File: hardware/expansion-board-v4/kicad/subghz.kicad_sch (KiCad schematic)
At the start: 32 parts, among them J5 U.FL_978, Q2 AO3401A, U10 CC1312R1F3RGZR, Y2 48MHz ABM8W-7pF, Y3 32.768kHz FC-135

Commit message: fix(v4): 晶振负载电容按实测 CL 重算——C19/C20→33pF，C68/C69→18pF
罩哥给出实际买到的三颗晶振型号，CL 全部查实：

    Y1  X322512MSB4SI              CL=20pF     立创/JLCPCB/Evelta 三处一致
    Y2  ABM8W-48.0000MHZ-7-D1X-T3  CL=7pF      型号里的「-7-」就是 CL
    Y3  Q13FC13500004 (FC-135)     CL=12.5pF   Epson 官方 IC 配套页

按 C = (CL − Cstray) × 2、Cstray 取 3pF 重算：

              原值          新值      原偏差              新偏差
    C19/C20   15/15pF   →   33/33pF   -9.50pF ≈ 95ppm    -0.50pF ≈ 5ppm
    C68/C69   12/15pF   →   18/18pF   -2.83pF ≈ 28ppm    -0.50pF ≈ 5ppm
                            ↑ 原值还**不对称**，降低起振裕度

Y3 的 28ppm ≈ RTC 每天走时差 2.4 秒；改后 0.43 秒。
Y1 的 95ppm 虽在 USB 全速 ±500ppm 内，但计时精度白损失一个数量级。
sheet_subghz.py 里原注释写着「32k 12/15pF 照抄」——就是照抄参考设计没算。

Y2 不需要外部负载电容（CC1312 片内电容阵列），但 CL=7pF 要在固件 CCFG 的
XOSC HF cap-array 里配，这是软件项，已在核对清单里标注。

## 验证过：Gerber 一个字节没变

value 字段在 F.Fab 层，位号在 F.Silkscreen 层，导出的 13 层不含 F.Fab。
逐文件比对（排除 CreationDate/ProjectId 等注释行）：
**15 个 Gerber/钻孔文件的图形指令完全一致，0 处差异**。已打样的文件不用重发。

## 🔴 顺带修了一个静默的缓存 bug

_fresh_netlist() 只比对顶层 expansion-board-v4.kicad_sch 的 mtime，
而元件都在 mcu/power/rf1090/sensors/subghz/interface 这些**子页**里。
改子页时顶层 mtime 不动 → 缓存判定"新鲜" → 拿旧网表出文档，**一声不吭**。

实测：子页改于 23:56，网表缓存停在 8-26 19:13，顶层原理图是 8-26 15:52
（比缓存还旧）。结果原理图和板子都更新了，BOM_PURCHASE.md 和 ASSEMBLY.md
却还印着 12pF/15pF。

改成比对**所有 .kicad_sch 的最新 mtime**。四个脚本都有这个函数，一并修了。
这跟 2026-08-23 那次 /tmp 缓存是同一类问题的第二种形态——上次修了"只判存在性
不判时间戳"，这次是"判了时间戳但判错了对象"。

gen_bom.py 的 PARTS 断言拦住了新值未归类，正是它该干的活。
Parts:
- C68: value 12pF -> 18pF
- C69: value 15pF -> 18pF
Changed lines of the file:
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@@
 			(effects (font (size 1.27 1.27)))
 		)
-		(property "Value" "12pF"
+		(property "Value" "18pF"
 			(at 203.2 154.94 0)
 			(effects (font (size 1.27 1.27)))
@@
 			(effects (font (size 1.27 1.27)))
 		)
-		(property "Value" "15pF"
+		(property "Value" "18pF"
 			(at 215.9 154.94 0)
 			(effects (font (size 1.27 1.27)))

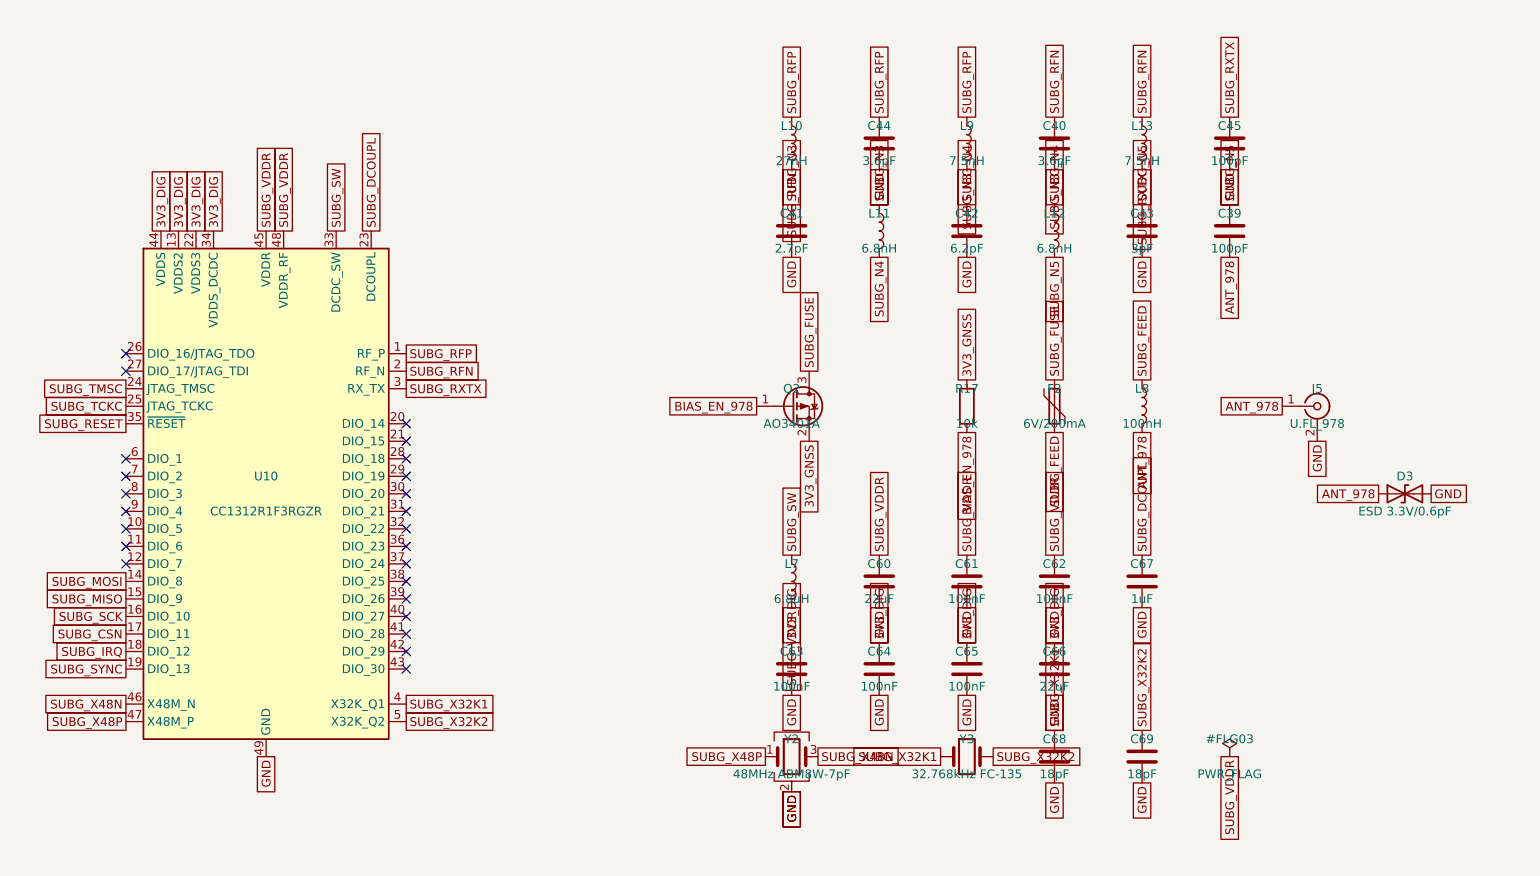
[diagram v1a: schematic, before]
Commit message: fix(v4): finalize V4.3 board after manual routing
罩哥手工完成全部布线后的定稿。DRC 0 violations / 0 unconnected。

板子本身:
- 1607 段走线 / 415 个过孔 / 207 个封装 / 15 个 zone
- RP_1V1 在 B.Cu 合并为单块 228.96mm2，四颗 RP_1V1 去耦落入其中
- C81 挪到 U12 旁 1.47mm(原 3.36mm)，脚下由「无铜」变为落在 B.Cu 的 3V3_RF 上
- U8.23(DVDD) 补一个 RP_1V1 过孔 @(85.798,72.600)，接入距离 1.63 -> 0.88mm
  落点在既有走线上，未改任何走线；与相邻 QFN 焊盘边缘间距 +0.312mm

原理图:
- rf1090 的 PWR_FLAG 由 #FLG05 改为 #FLG06。sheet_power.py 已占用 #FLG05,
  两页撞号会让网表导出报「批注错误」。改后网表 714 节点、网络归属零变化。

.kicad_pro 保留正式板原有的 FINE netclass(0.13mm, 用于 DEMOD0-3/RECOVERED_CLK/
SWCLK/SWDIO)。板上这 7 个网络实际都按 0.15mm 布线、FINE 处于闲置; 两份工程
文件下各跑一次 DRC 均为 0，且 drc_exclusions 都是空的。
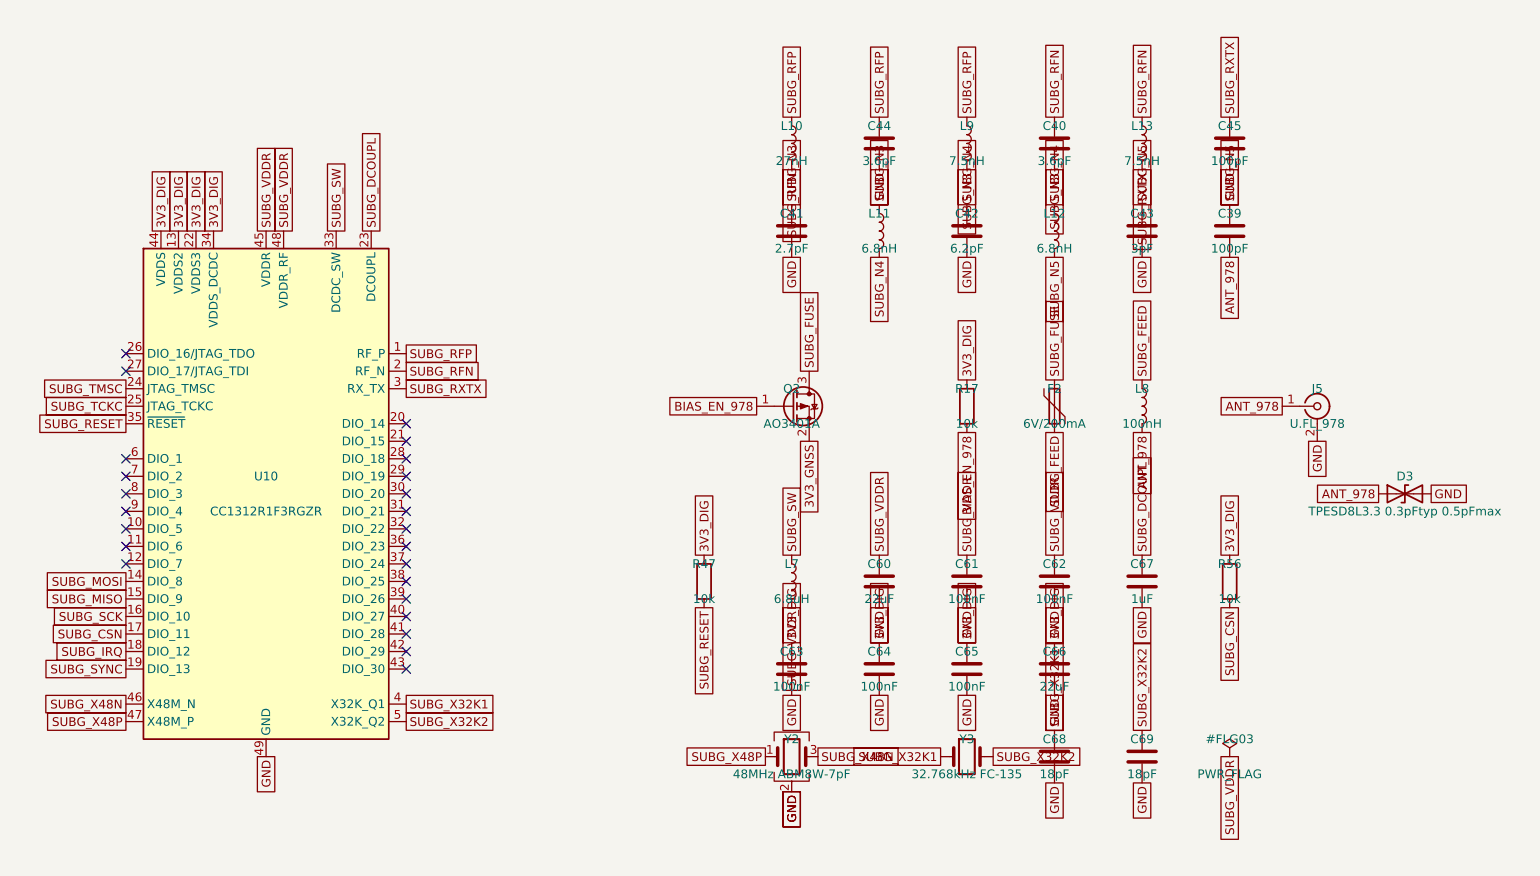
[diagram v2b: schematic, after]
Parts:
- added R47, R56: 10k, Resistor_SMD:R_0603_1608Metric, symbol Device:R
- D3: value ESD 3.3V/0.6pF -> TPESD8L3.3 0.3pFtyp 0.5pFmax
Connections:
- net 3V3_DIG: now also R17.1, R47.1, R56.1
- net 3V3_GNSS: no longer R17.1
- net SUBG_CSN: now also R56.2
- net SUBG_RESET: now also R47.2
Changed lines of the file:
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@@
+	)
+	(symbol
+		(lib_id "Device:R")
+		(at 152.4 127 0)
+		(unit 1)
+		(exclude_from_sim no)
+		(in_bom yes)
+		(on_board yes)
+		(dnp no)
+		(property "Reference" "R47"
+			(at 152.4 124.46 0)
+			(effects (font (size 1.27 1.27)))
+		)
+		(property "Value" "10k"
+			(at 152.4 129.54 0)
+			(effects (font (size 1.27 1.27)))
+		)
+		(property "Footprint" "Resistor_SMD:R_0603_1608Metric"
+			(at 152.4 132.08 0)
+			(effects (font (size 1.27 1.27))
+				(hide yes))
+		)
+		(property "Datasheet" "~"
+			(at 152.4 134.62 0)
+			(effects (font (size 1.27 1.27))
+				(hide yes))
+		)
+		(pin "1"
+		)
+		(pin "2"
+		)
+		(instances
+			(project "expansion-board-v4"
+				(path "/10000000-0000-4000-8000-000000000001/20000000-0000-4000-8000-000000000004"
+					(reference "R47")
+					(unit 1)
+				)
+			)
+		)
+	)
+	(global_label "3V3_DIG"
+		(shape passive)
+		(at 152.4 123.19 270)
+		(effects (font (size 1.27 1.27)) (justify left))
+	)
+	(global_label "SUBG_RESET"
+		(shape passive)
+		(at 152.4 130.81 90)
+		(effects (font (size 1.27 1.27)) (justify right))
+	)
+	(symbol
+		(lib_id "Device:R")
+		(at 228.6 127 0)
+		(unit 1)
+		(exclude_from_sim no)
+		(in_bom yes)
+		(on_board yes)
+		(dnp no)
+		(property "Reference" "R56"
+			(at 228.6 124.46 0)
+			(effects (font (size 1.27 1.27)))
+		)
+		(property "Value" "10k"
+			(at 228.6 129.54 0)
+			(effects (font (size 1.27 1.27)))
+		)
+		(property "Footprint" "Resistor_SMD:R_0603_1608Metric"
+			(at 228.6 132.08 0)
+			(effects (font (size 1.27 1.27))
+				(hide yes))
+		)
+		(property "Datasheet" "~"
+			(at 228.6 134.62 0)
+			(effects (font (size 1.27 1.27))
+				(hide yes))
+		)
+		(pin "1"
+		)
+		(pin "2"
+		)
+		(instances
+			(project "expansion-board-v4"
+				(path "/10000000-0000-4000-8000-000000000001/20000000-0000-4000-8000-000000000004"
+					(reference "R56")
+					(unit 1)
+				)
+			)
+		)
+	)
+	(global_label "3V3_DIG"
+		(shape passive)
+		(at 228.6 123.19 270)
+		(effects (font (size 1.27 1.27)) (justify left))
+	)
+	(global_label "SUBG_CSN"
+		(shape passive)
+		(at 228.6 130.81 90)
+		(effects (font (size 1.27 1.27)) (justify right))
 	)
 	(symbol
@@
 		)
 	)
-	(global_label "3V3_GNSS"
+	(global_label "3V3_DIG"
 		(shape passive)
 		(at 190.5 97.79 270)
@@
 			(effects (font (size 1.27 1.27)))
 		)
-		(property "Value" "ESD 3.3V/0.6pF"
+		(property "Value" "TPESD8L3.3 0.3pFtyp 0.5pFmax"
 			(at 254 116.84 0)
 			(effects (font (size 1.27 1.27)))

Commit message: hardware(v4.7): 修正 C99 并刷新整套制造与装配文件
在用户修订的布局上将 C99 改为 100nF/0402，复用 C37/C52 的 C307331；同步原理图版本、BOM/CPL、装配图、安装助手及制造归档，更新下单入口和未决电气项。

验证：DRC 0 违规/0 未连通，存盘覆铜与包源一致性已核对；提交前版本包/安装助手20项，18通过、2跳过。元件契约中已记录的 C84 两条子断言失败按用户范围保留；Y4 供电和 U22 VREF 建议尚待闭环。内部工具、审计报告和采购过程文件按仓库规则仅留本地。
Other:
- title: Expansion Board V1 - 978MHz UAT: CC1312R -> Expansion Board V4.7 - 978MHz UAT: CC1312R
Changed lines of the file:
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@@
 	(paper "A3")
 	(title_block
-		(title "Expansion Board V1 - 978MHz UAT: CC1312R")
+		(title "Expansion Board V4.7 - 978MHz UAT: CC1312R")
 		(date "2026-08-01")
-		(rev "V1")
+		(rev "V4.7")
 		(company "Pilot Kit")
 	)

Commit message: feat(v4.11): 固化扩展板并修正电池补偿
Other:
- title: Expansion Board V4.7 - 978MHz UAT: CC1312R -> Expansion Board V4.11 - 978MHz UAT: CC1312R
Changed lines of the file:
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@@
 	(paper "A3")
 	(title_block
-		(title "Expansion Board V4.7 - 978MHz UAT: CC1312R")
+		(title "Expansion Board V4.11 - 978MHz UAT: CC1312R")
 		(date "2026-08-01")
-		(rev "V4.7")
+		(rev "V4.11")
 		(company "Pilot Kit")
 	)
